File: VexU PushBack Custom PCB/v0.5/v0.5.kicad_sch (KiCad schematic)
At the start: 39 parts, among them J1 4P4C, J2 Conn_01x04_Pin, U1 Teensy4.1, U2 MP2338GTL-P, U3 4069, U4 MAX485E

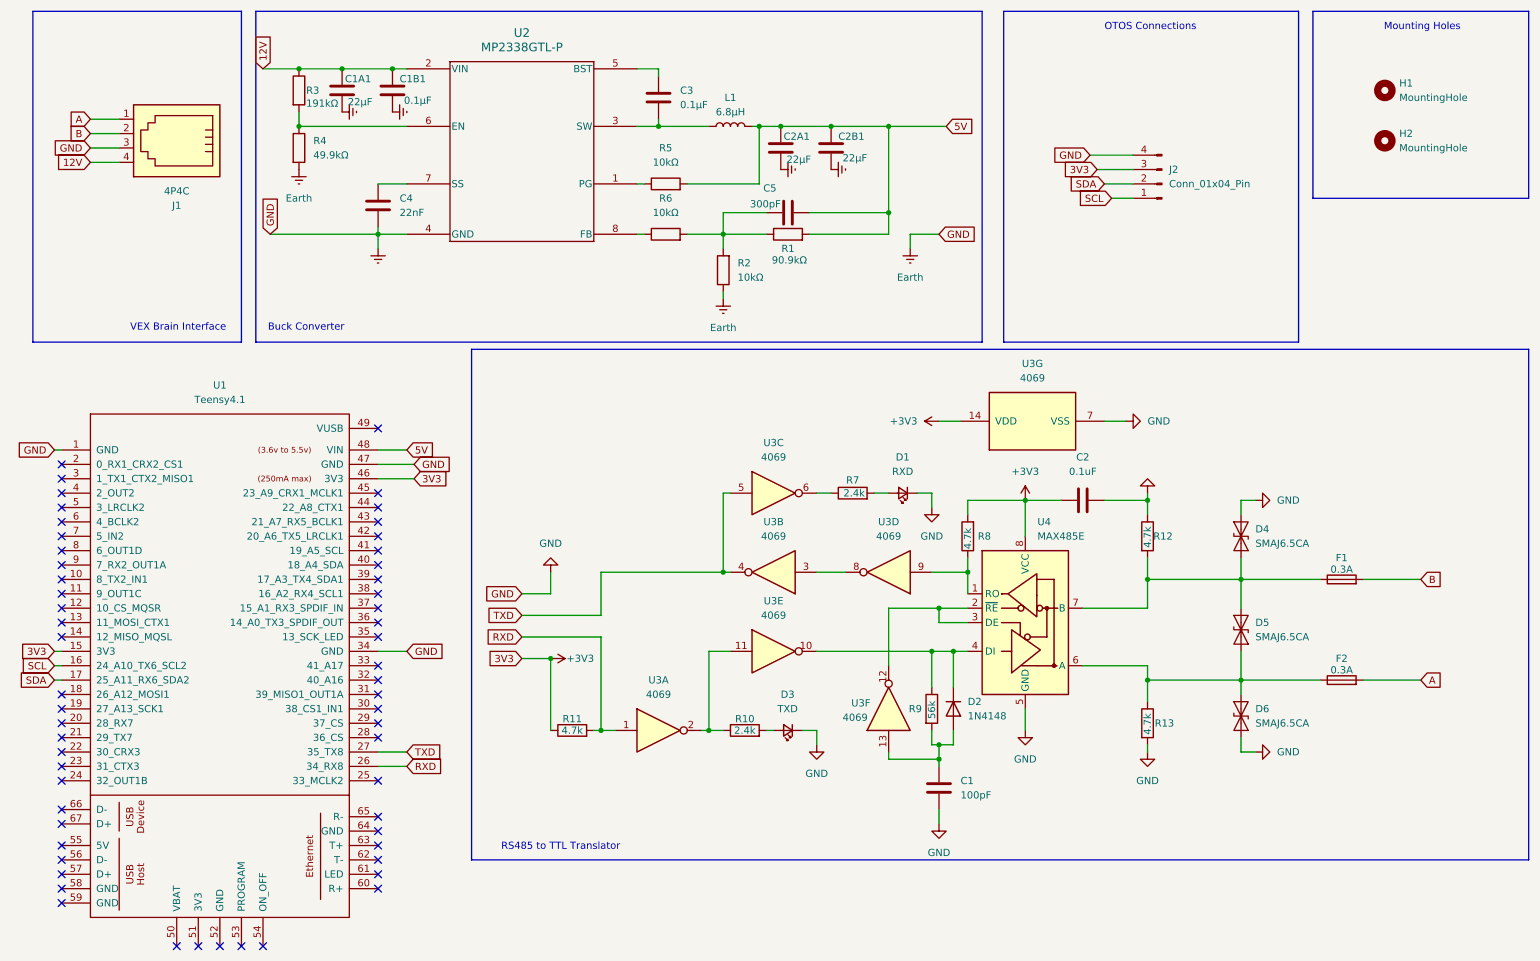
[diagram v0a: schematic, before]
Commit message: Updating Footprints & Symbols
Updating Main branch with updated footprints & symbols before branching
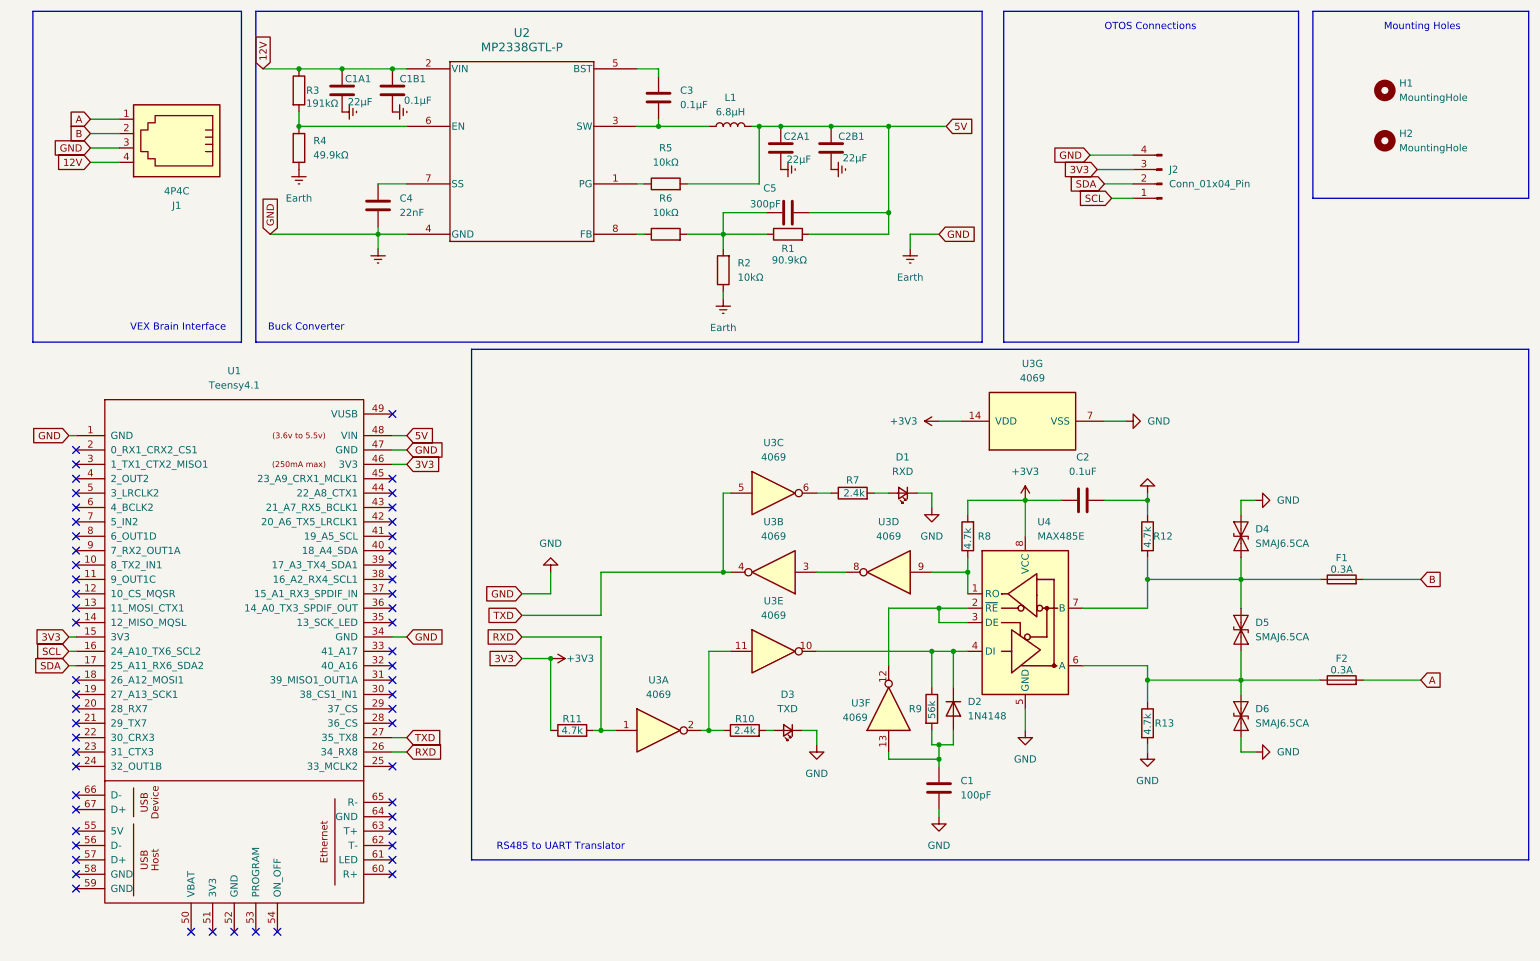
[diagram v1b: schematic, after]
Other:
- note added: "RS485 to UART Translator"
- note removed: "RS485 to TTL Translator"
- moved on the sheet: U1

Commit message: Finishied Schematic
Start work on 4 layer board tracing
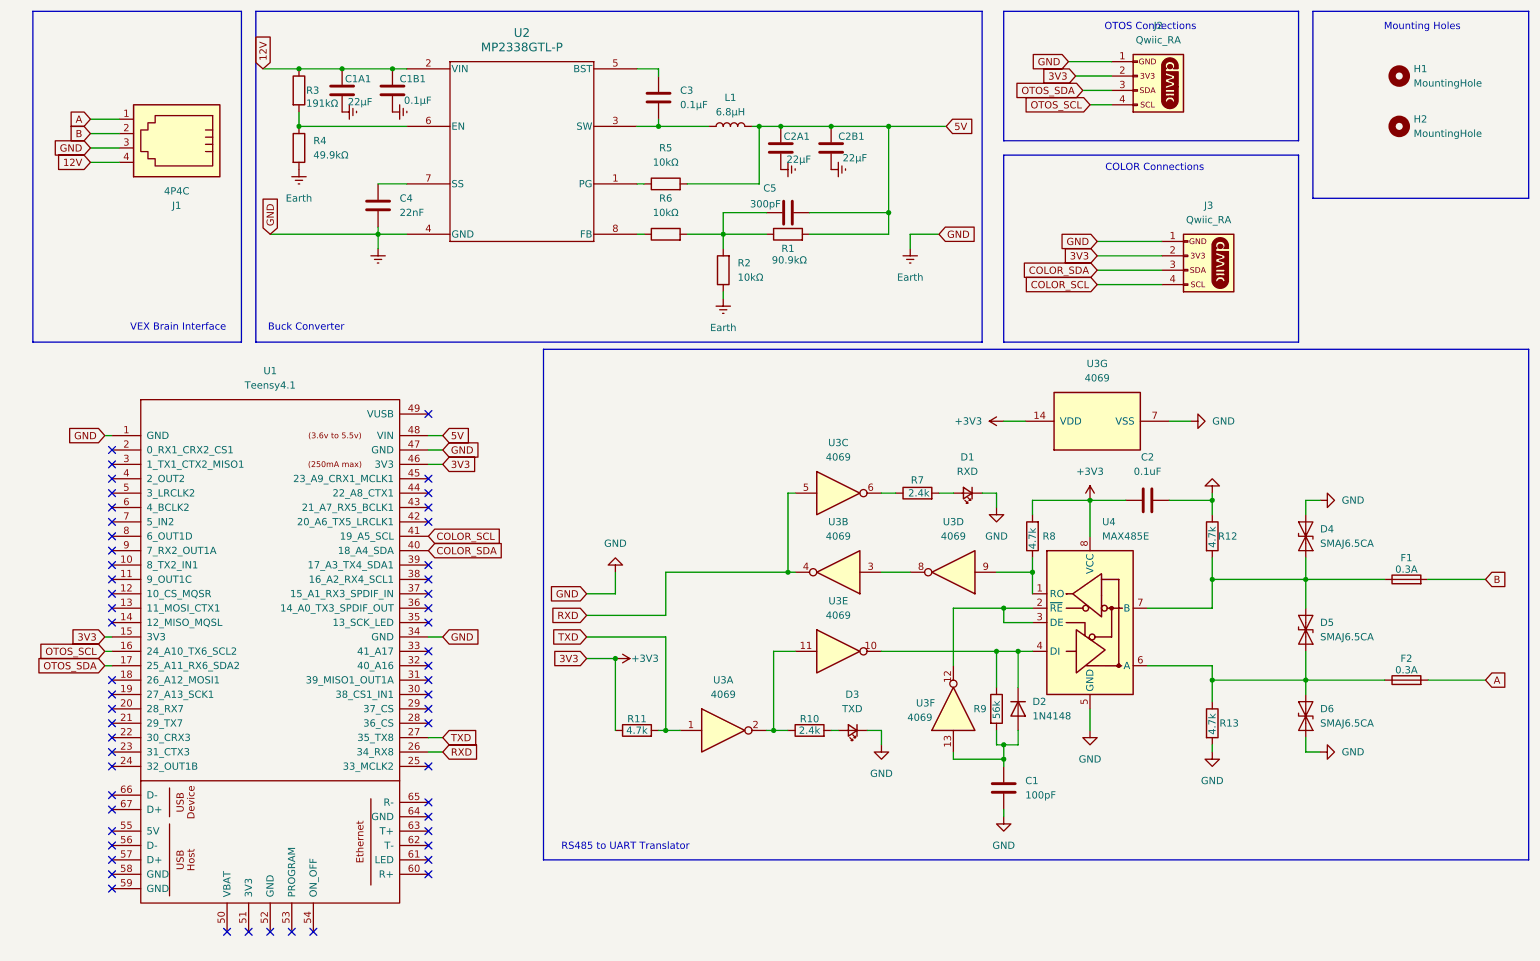
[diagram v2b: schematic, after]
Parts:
- removed J2: Conn_01x04_Pin, Connector_PinHeader_1.27mm:PinHeader_1x04_P1.27mm_Horizontal, symbol Connector:Conn_01x04_Pin
- added J2, J3: Qwiic_RA, SparkFun-Connector:JST_1x04_P1.0mm_Horizontal_SMD, symbol SparkFun-Connector:Qwiic_Horizontal
- H1, H2: footprint MountingHole:MountingHole_2.2mm_M2 -> MountingHole:MountingHole_3.2mm_M3
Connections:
- net +3V3: now also J2.2 (Pin_2), J3.2 (Pin_2)
- net Earth: now also J2.1 (Pin_1), J3.1 (Pin_1)
- net RXD: now also U3.4, U3.5; no longer R11.2, U3.1
- net TXD: now also R11.2, U3.1; no longer U3.4, U3.5
- net COLOR_SDA: now reaches U1.40 (18_A4_SDA)
- net COLOR_SDA: now also J3.3 (Pin_3)
- net COLOR_SCL: now reaches U1.41 (19_A5_SCL)
- net COLOR_SCL: now also J3.4 (Pin_4)
- net SCL renamed OTOS_SCL
- net OTOS_SCL: now also J2.4 (Pin_4)
- net SDA renamed OTOS_SDA
- net OTOS_SDA: now also J2.3 (Pin_3)
- no-connect marks 57 -> 55
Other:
- note added: "COLOR Connections"
- moved on the sheet: C1, C2, D1, D2, D3, D4, D5, D6, F1, F2, R10, R11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

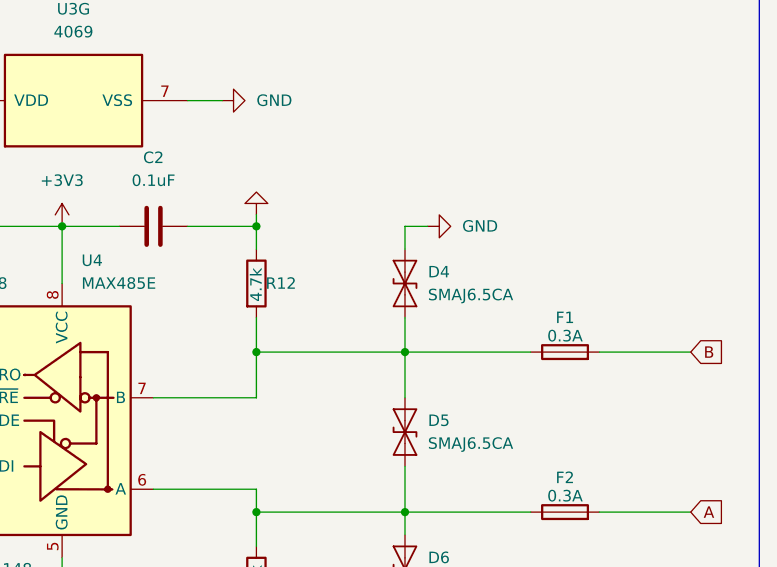
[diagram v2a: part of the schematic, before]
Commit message: Finished Routing PCB
Pushed For production
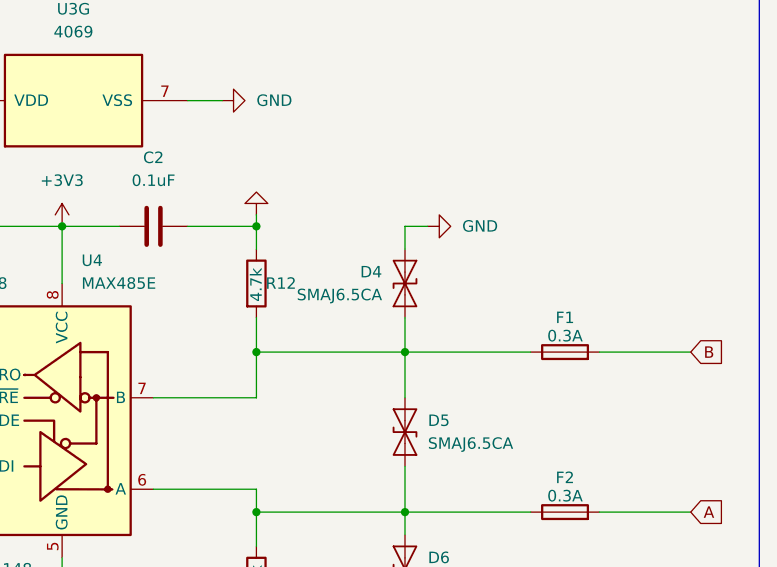
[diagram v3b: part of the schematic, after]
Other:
- moved on the sheet: D4
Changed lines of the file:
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@@
 	(symbol
 		(lib_id "Diode:SMAJ6.5CA")
-		(at 242.57 107.95 270)
+		(at 242.57 107.95 90)
+		(mirror x)
 		(unit 1)
 		(exclude_from_sim no)
@@
 		(on_board yes)
 		(dnp no)
-		(fields_autoplaced yes)
 		(property "Reference" "D4"
-			(at 245.11 106.6799 90)
+			(at 240.03 106.6799 90)
 			(effects
 				(font
@@
 		)
 		(property "Value" "SMAJ6.5CA"
-			(at 245.11 109.2199 90)
+			(at 240.03 109.2199 90)
 			(effects
 				(font
@@
 		)
 		(property "Footprint" "Diode_SMD:D_SMA"
-			(at 237.49 107.95 0)
+			(at 247.65 107.95 0)
 			(effects
 				(font
